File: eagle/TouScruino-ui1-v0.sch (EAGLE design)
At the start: 8 parts, among them U1 TFT_20

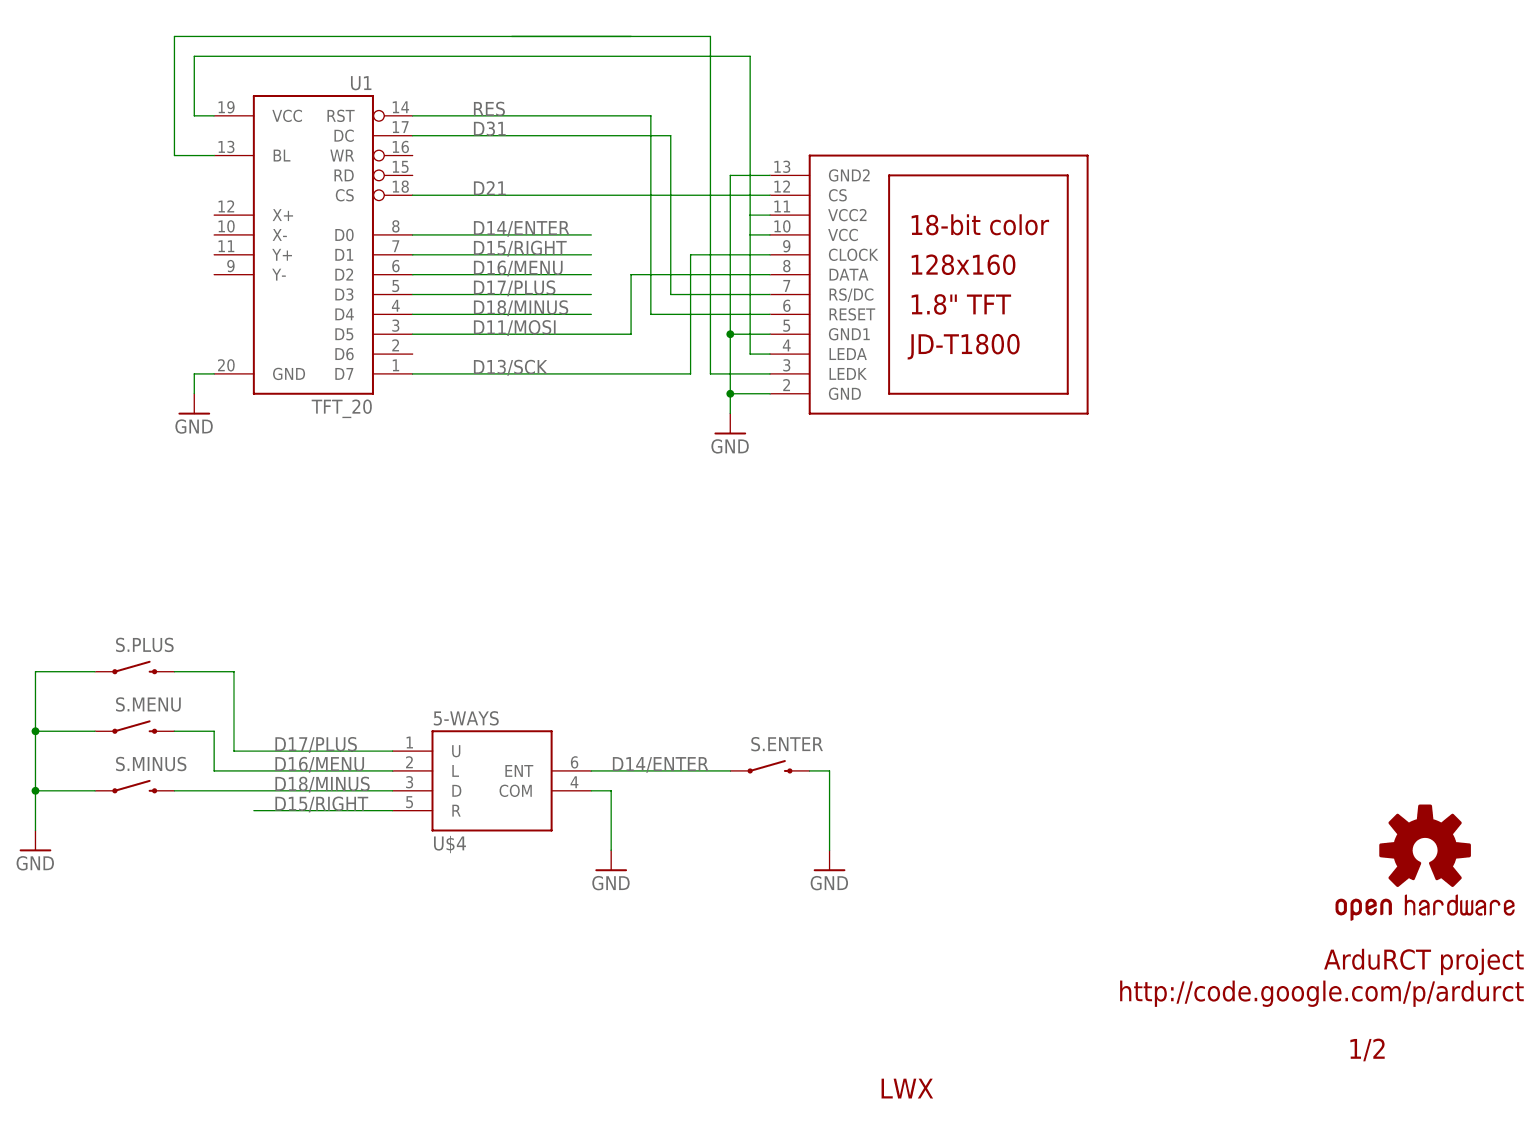
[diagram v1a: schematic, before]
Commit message: 
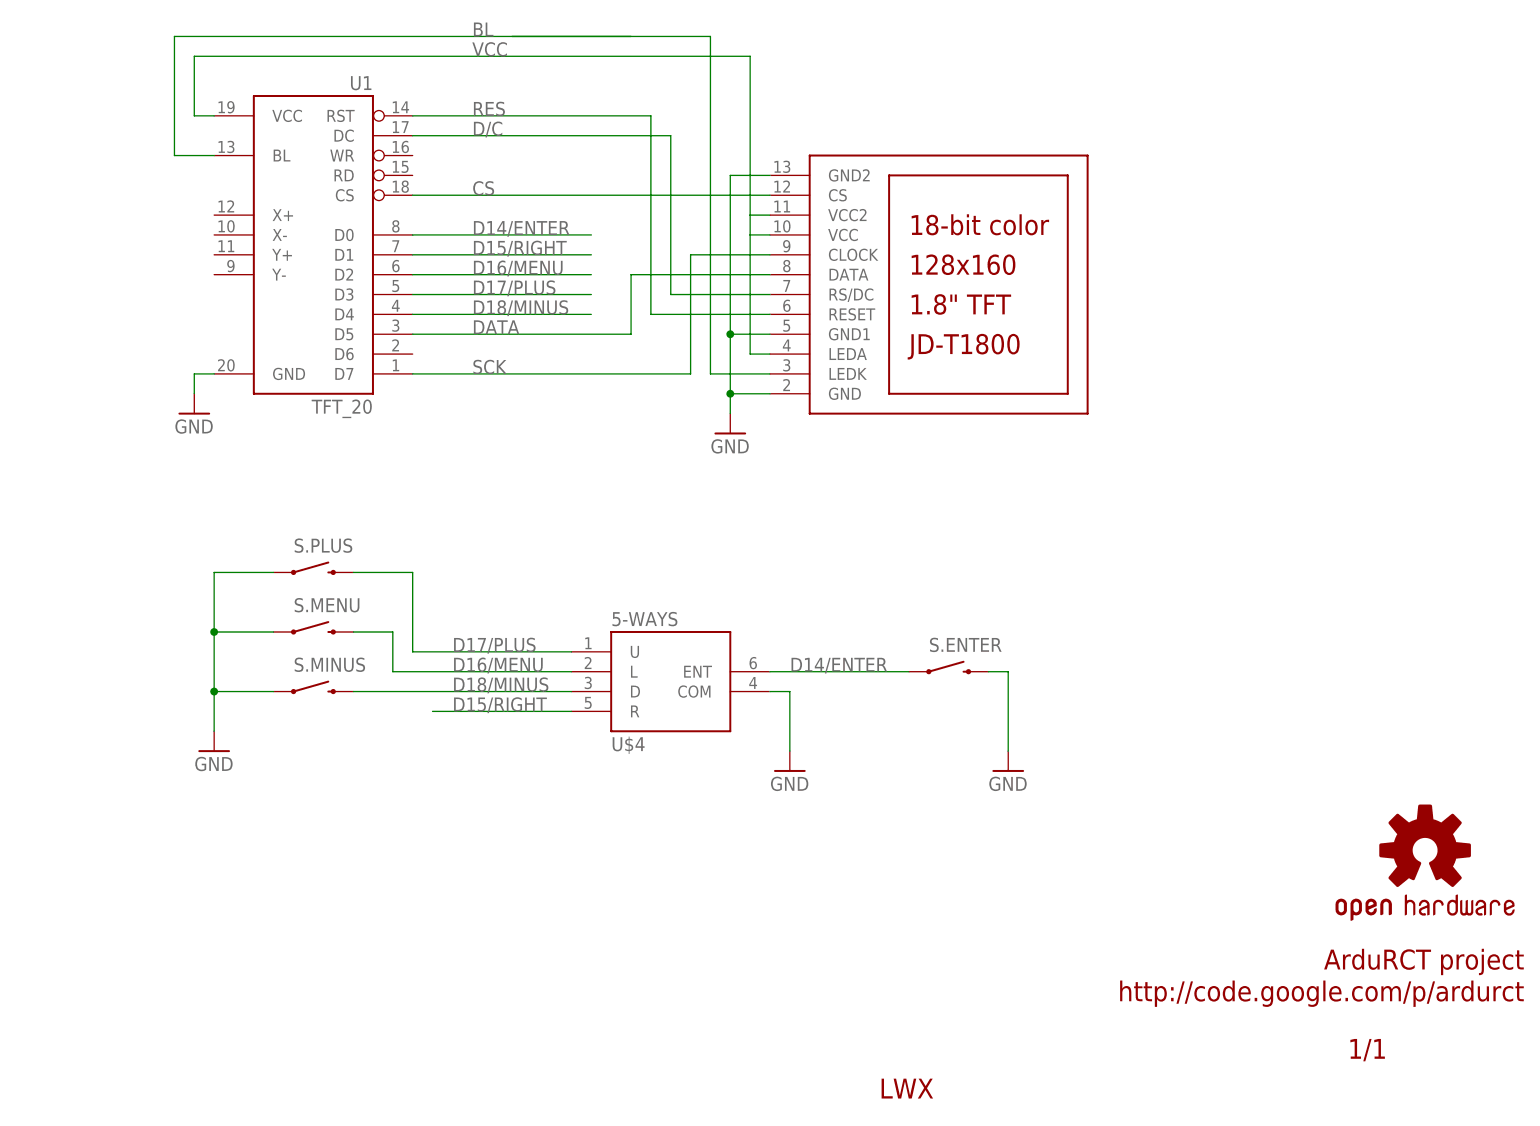
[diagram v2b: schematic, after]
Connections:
- net D11/MOSI renamed DATA
- net D13/SCK renamed SCK
- net D21 renamed CS
- net D31 renamed D/C
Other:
- note added: "1/1"
- note removed: "1/2"
- moved on the sheet: S.ENTER, S.MENU, S.MINUS, S.PLUS, U$4
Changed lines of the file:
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@@
 <plain>
 <text x="161.29" y="1.27" size="2.54" layer="94" font="vector">LWX</text>
-<text x="221.234" y="6.35" size="2.54" layer="94" font="vector">1/2</text>
+<text x="221.234" y="6.35" size="2.54" layer="94" font="vector">1/1</text>
 <text x="243.84" y="20.32" size="2.54" layer="94" ratio="12" rot="R180">ArduRCT project</text>
 <text x="243.84" y="16.256" size="2.54" layer="94" ratio="12" rot="R180">http://code.google.com/p/ardurct</text>
@@
 <instance part="U1" gate="G$1" x="88.9" y="111.76" rot="MR0"/>
 <instance part="GND1" gate="1" x="73.66" y="88.9"/>
-<instance part="U$4" gate="G$1" x="111.76" y="43.18"/>
-<instance part="GND12" gate="1" x="127" y="30.48"/>
-<instance part="S.ENTER" gate="G$1" x="147.32" y="43.18"/>
-<instance part="S.PLUS" gate="G$1" x="66.04" y="55.88"/>
-<instance part="S.MINUS" gate="G$1" x="66.04" y="40.64"/>
-<instance part="S.MENU" gate="G$1" x="66.04" y="48.26"/>
-<instance part="GND18" gate="1" x="53.34" y="33.02"/>
-<instance part="GND21" gate="1" x="154.94" y="30.48"/>
+<instance part="U$4" gate="G$1" x="134.62" y="55.88"/>
+<instance part="GND12" gate="1" x="149.86" y="43.18"/>
+<instance part="S.ENTER" gate="G$1" x="170.18" y="55.88"/>
+<instance part="S.PLUS" gate="G$1" x="88.9" y="68.58"/>
+<instance part="S.MINUS" gate="G$1" x="88.9" y="53.34"/>
+<instance part="S.MENU" gate="G$1" x="88.9" y="60.96"/>
+<instance part="GND18" gate="1" x="76.2" y="45.72"/>
+<instance part="GND21" gate="1" x="177.8" y="43.18"/>
 <instance part="GND15" gate="1" x="142.24" y="86.36"/>
 <instance part="LCD1" gate="G$1" x="170.18" y="106.68" rot="MR180"/>
@@
 <pinref part="LCD1" gate="G$1" pin="LEDA"/>
 <wire x1="144.78" y1="96.52" x2="147.32" y2="96.52" width="0.1524" layer="91"/>
+<label x="109.22" y="134.62" size="1.778" layer="95"/>
 </segment>
 </net>
@@
 <wire x1="139.7" y1="93.98" x2="139.7" y2="137.16" width="0.1524" layer="91"/>
 <wire x1="139.7" y1="137.16" x2="71.12" y2="137.16" width="0.1524" layer="91"/>
+<label x="109.22" y="137.16" size="1.778" layer="95"/>
 </segment>
 </net>
@@
 <segment>
 <pinref part="U$4" gate="G$1" pin="COM"/>
-<wire x1="124.46" y1="40.64" x2="127" y2="40.64" width="0.1524" layer="91"/>
-<wire x1="127" y1="40.64" x2="127" y2="33.02" width="0.1524" layer="91"/>
+<wire x1="147.32" y1="53.34" x2="149.86" y2="53.34" width="0.1524" layer="91"/>
+<wire x1="149.86" y1="53.34" x2="149.86" y2="45.72" width="0.1524" layer="91"/>
 <pinref part="GND12" gate="1" pin="GND"/>
 </segment>
 <segment>
 <pinref part="GND18" gate="1" pin="GND"/>
-<wire x1="53.34" y1="55.88" x2="53.34" y2="48.26" width="0.1524" layer="91"/>
+<wire x1="76.2" y1="68.58" x2="76.2" y2="60.96" width="0.1524" layer="91"/>
 <pinref part="S.MINUS" gate="G$1" pin="1"/>
-<wire x1="53.34" y1="48.26" x2="53.34" y2="40.64" width="0.1524" layer="91"/>
-<wire x1="53.34" y1="40.64" x2="53.34" y2="35.56" width="0.1524" layer="91"/>
-<wire x1="60.96" y1="40.64" x2="53.34" y2="40.64" width="0.1524" layer="91"/>
+<wire x1="76.2" y1="60.96" x2="76.2" y2="53.34" width="0.1524" layer="91"/>
+<wire x1="76.2" y1="53.34" x2="76.2" y2="48.26" width="0.1524" layer="91"/>
+<wire x1="83.82" y1="53.34" x2="76.2" y2="53.34" width="0.1524" layer="91"/>
 <pinref part="S.MENU" gate="G$1" pin="1"/>
-<wire x1="60.96" y1="48.26" x2="53.34" y2="48.26" width="0.1524" layer="91"/>
+<wire x1="83.82" y1="60.96" x2="76.2" y2="60.96" width="0.1524" layer="91"/>
 <pinref part="S.PLUS" gate="G$1" pin="1"/>
-<wire x1="60.96" y1="55.88" x2="53.34" y2="55.88" width="0.1524" layer="91"/>
-<junction x="53.34" y="48.26"/>
-<junction x="53.34" y="40.64"/>
+<wire x1="83.82" y1="68.58" x2="76.2" y2="68.58" width="0.1524" layer="91"/>
+<junction x="76.2" y="60.96"/>
+<junction x="76.2" y="53.34"/>
 </segment>
 <segment>
 <pinref part="GND21" gate="1" pin="GND"/>
-<wire x1="154.94" y1="43.18" x2="154.94" y2="33.02" width="0.1524" layer="91"/>
+<wire x1="177.8" y1="55.88" x2="177.8" y2="45.72" width="0.1524" layer="91"/>
 <pinref part="S.ENTER" gate="G$1" pin="2"/>
-<wire x1="152.4" y1="43.18" x2="154.94" y2="43.18" width="0.1524" layer="91"/>
+<wire x1="175.26" y1="55.88" x2="177.8" y2="55.88" width="0.1524" layer="91"/>
 </segment>
 <segment>
@@
 </segment>
 </net>
-<net name="D31" class="0">
+<net name="D/C" class="0">
 <segment>
 <pinref part="U1" gate="G$1" pin="DC"/>
@@
 </segment>
 </net>
-<net name="D21" class="0">
+<net name="CS" class="0">
 <segment>
 <pinref part="U1" gate="G$1" pin="CS"/>
@@
 </segment>
 <segment>
-<label x="83.82" y="40.64" size="1.778" layer="95"/>
-<wire x1="71.12" y1="40.64" x2="99.06" y2="40.64" width="0.1524" layer="91"/>
+<label x="106.68" y="53.34" size="1.778" layer="95"/>
+<wire x1="93.98" y1="53.34" x2="121.92" y2="53.34" width="0.1524" layer="91"/>
 <pinref part="U$4" gate="G$1" pin="D"/>
 <pinref part="S.MINUS" gate="G$1" pin="2"/>
@@
 <net name="D14/ENTER" class="0">
 <segment>
-<label x="127" y="43.18" size="1.778" layer="95"/>
-<wire x1="124.46" y1="43.18" x2="142.24" y2="43.18" width="0.1524" layer="91"/>
+<label x="149.86" y="55.88" size="1.778" layer="95"/>
+<wire x1="147.32" y1="55.88" x2="165.1" y2="55.88" width="0.1524" layer="91"/>
 <pinref part="U$4" gate="G$1" pin="ENT"/>
 <pinref part="S.ENTER" gate="G$1" pin="1"/>
@@
 <net name="D15/RIGHT" class="0">
 <segment>
-<label x="83.82" y="38.1" size="1.778" layer="95"/>
-<wire x1="81.28" y1="38.1" x2="99.06" y2="38.1" width="0.1524" layer="91"/>
+<label x="106.68" y="50.8" size="1.778" layer="95"/>
+<wire x1="104.14" y1="50.8" x2="121.92" y2="50.8" width="0.1524" layer="91"/>
 <pinref part="U$4" gate="G$1" pin="R"/>
 </segment>
@@
 <net name="D17/PLUS" class="0">
 <segment>
-<label x="83.82" y="45.72" size="1.778" layer="95"/>
-<wire x1="78.74" y1="45.72" x2="99.06" y2="45.72" width="0.1524" layer="91"/>
+<label x="106.68" y="58.42" size="1.778" layer="95"/>
+<wire x1="101.6" y1="58.42" x2="121.92" y2="58.42" width="0.1524" layer="91"/>
 <pinref part="U$4" gate="G$1" pin="U"/>
 <pinref part="S.PLUS" gate="G$1" pin="2"/>
-<wire x1="71.12" y1="55.88" x2="78.74" y2="55.88" width="0.1524" layer="91"/>
-<wire x1="78.74" y1="55.88" x2="78.74" y2="45.72" width="0.1524" layer="91"/>
+<wire x1="93.98" y1="68.58" x2="101.6" y2="68.58" width="0.1524" layer="91"/>
+<wire x1="101.6" y1="68.58" x2="101.6" y2="58.42" width="0.1524" layer="91"/>
 </segment>
 <segment>
@@
 <net name="D16/MENU" class="0">
 <segment>
-<wire x1="76.2" y1="43.18" x2="99.06" y2="43.18" width="0.1524" layer="91"/>
-<label x="83.82" y="43.18" size="1.778" layer="95"/>
+<wire x1="99.06" y1="55.88" x2="121.92" y2="55.88" width="0.1524" layer="91"/>
+<label x="106.68" y="55.88" size="1.778" layer="95"/>
 <pinref part="U$4" gate="G$1" pin="L"/>
 <pinref part="S.MENU" gate="G$1" pin="2"/>
-<wire x1="71.12" y1="48.26" x2="76.2" y2="48.26" width="0.1524" layer="91"/>
-<wire x1="76.2" y1="48.26" x2="76.2" y2="43.18" width="0.1524" layer="91"/>
+<wire x1="93.98" y1="60.96" x2="99.06" y2="60.96" width="0.1524" layer="91"/>
+<wire x1="99.06" y1="60.96" x2="99.06" y2="55.88" width="0.1524" layer="91"/>
 </segment>
 <segment>
@@
 </segment>
 </net>
-<net name="D11/MOSI" class="0">
+<net name="DATA" class="0">
 <segment>
 <pinref part="U1" gate="G$1" pin="D5"/>
@@
 </segment>
 </net>
-<net name="D13/SCK" class="0">
+<net name="SCK" class="0">
 <segment>
 <pinref part="U1" gate="G$1" pin="D7"/>
